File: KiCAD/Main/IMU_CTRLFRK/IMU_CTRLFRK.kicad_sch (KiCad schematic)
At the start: 13 parts, among them U3 LIS2MDL, U7 ISM6HG256x

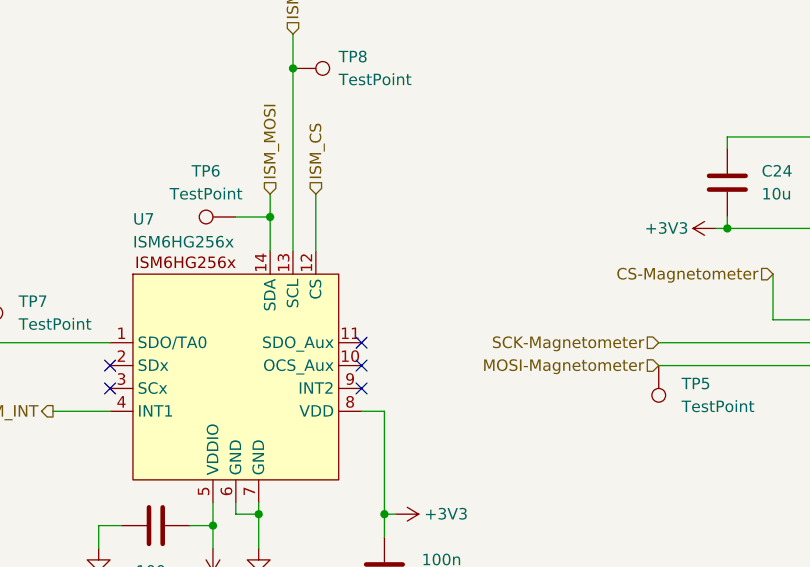
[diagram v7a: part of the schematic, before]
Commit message: Edit PCB Layout to increase min hole size and decrease price, prepare production files, prepare for main branch merge
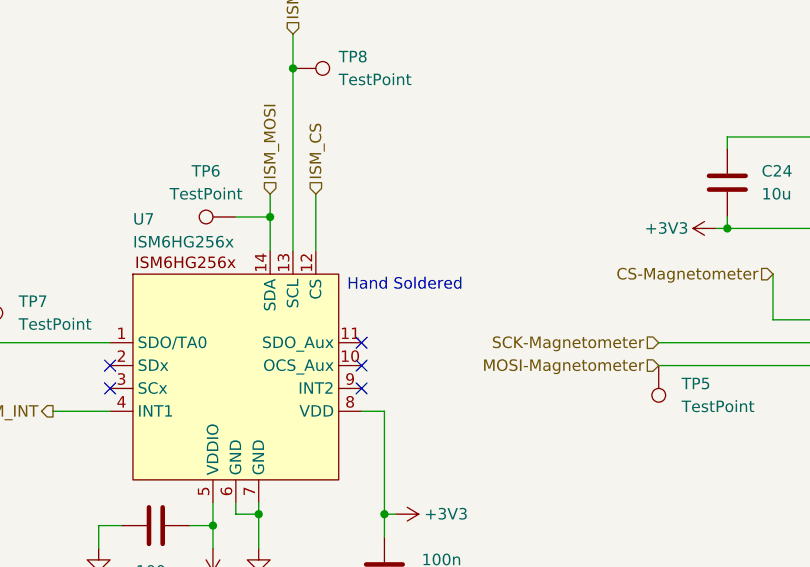
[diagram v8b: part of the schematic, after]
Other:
- note added: "Hand Soldered"
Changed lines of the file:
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@@
 	(generator_version "9.0")
 	(paper "A4")
+	(text "Hand Soldered\n"
+		(exclude_from_sim no)
+		(at 129.286 93.98 0)
+		(effects
+			(font
+				(size 1.27 1.27)
+			)
+		)
+	)
 	(junction
 		(at 165.1 87.63)
